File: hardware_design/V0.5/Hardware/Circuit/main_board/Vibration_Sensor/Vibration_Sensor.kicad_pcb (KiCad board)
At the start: 2 copper layers, 65 x 37.6 mm, 16 parts, among them U1 power_input, U5 main_board_top_rail

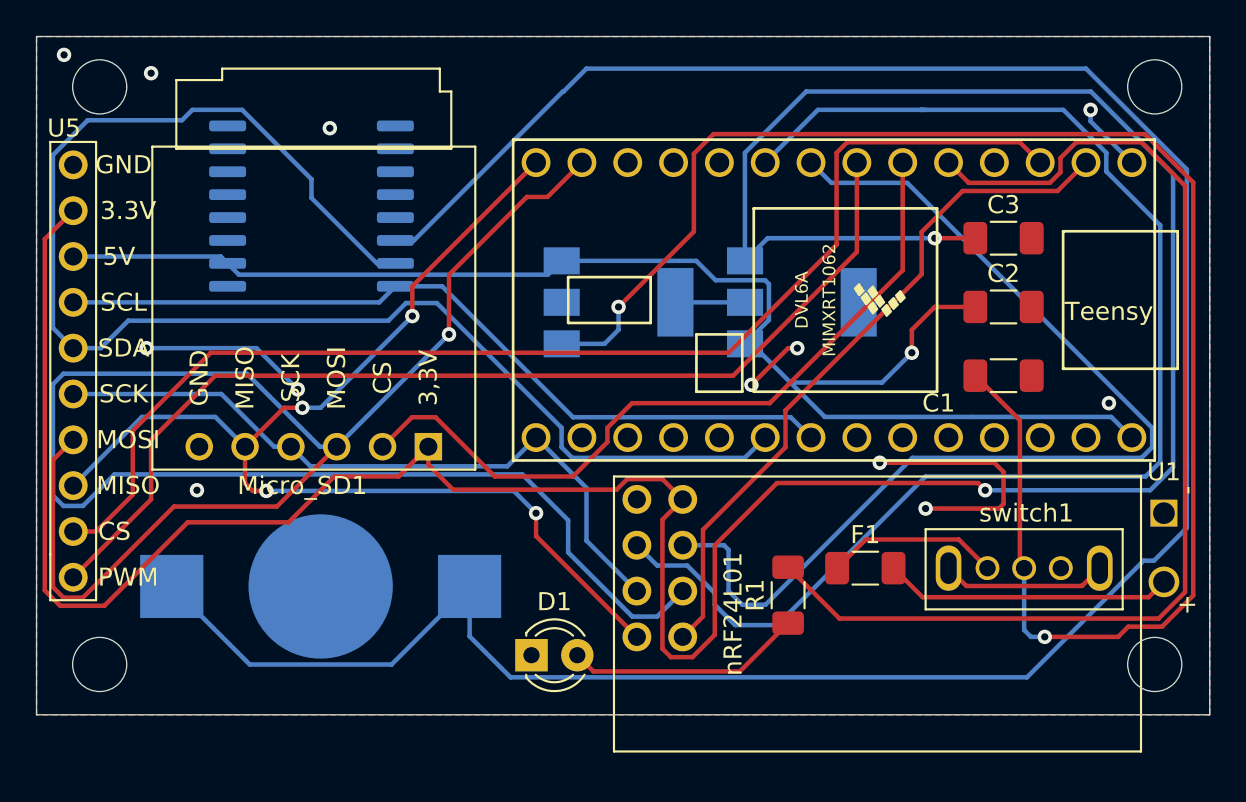
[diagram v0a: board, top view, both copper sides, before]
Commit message: Changed V0.5 PCB
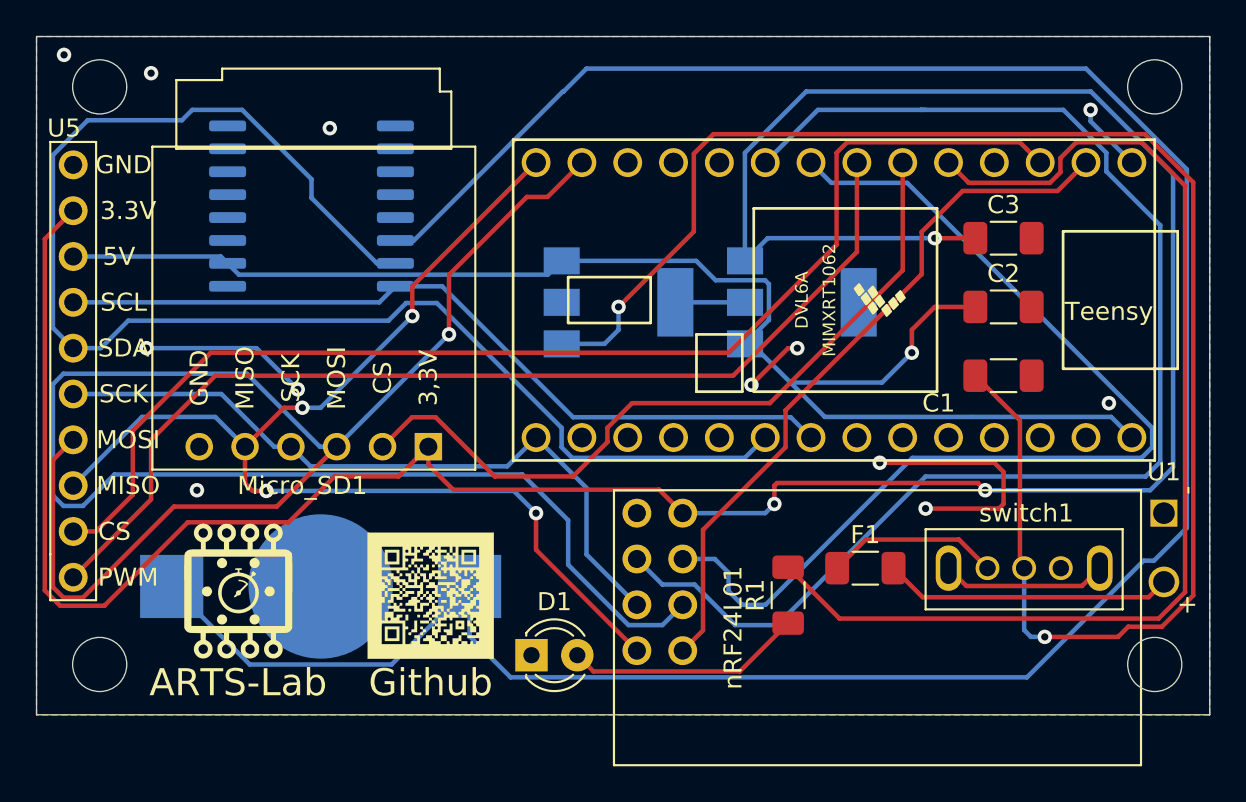
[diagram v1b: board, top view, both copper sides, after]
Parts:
- added ARTS-Lab: LOGO, graphics:GreyLabLogo, F.Cu at (129.0, 116.1)
- added Github: LOGO, graphics:SensorGit, F.Cu at (139.7, 116.3)
- moved nRF24L01 0.76 mm to (162.6, 118.1)
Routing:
- net Net-(C3-Pad1): track 171.6 -> 155.7 mm, vias 2 -> 3
- net Net-(U2-Pad8): track 58.4 -> 57.4 mm
- net Net-(U2-Pad2): track 38.6 -> 39.4 mm
- net Net-(Micro_SD1-Pad5): track 63.4 -> 64.2 mm
- net Net-(Micro_SD1-Pad4): track 38.8 -> 39.6 mm
- net Net-(U2-Pad9): track 74.7 -> 74.0 mm
- added copper zone on In1.Cu, net GND
- added copper zone on In1.Cu, net Net-(C2-Pad1)
- added copper zone on In2.Cu, net Net-(C3-Pad1)
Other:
- copper layers 2 -> 4
- net class Default removed
- board text added: "Ryan Yount Joud Satme Corinne Smith"
- board text added: "V0.5"
- board text removed: "Ryan Yount Joud Satme"
- board text removed: "V0.3.1"
